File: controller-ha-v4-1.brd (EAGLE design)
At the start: 120 x 75 mm, 55 parts, among them IC2 LM358MX, U1 DS1307

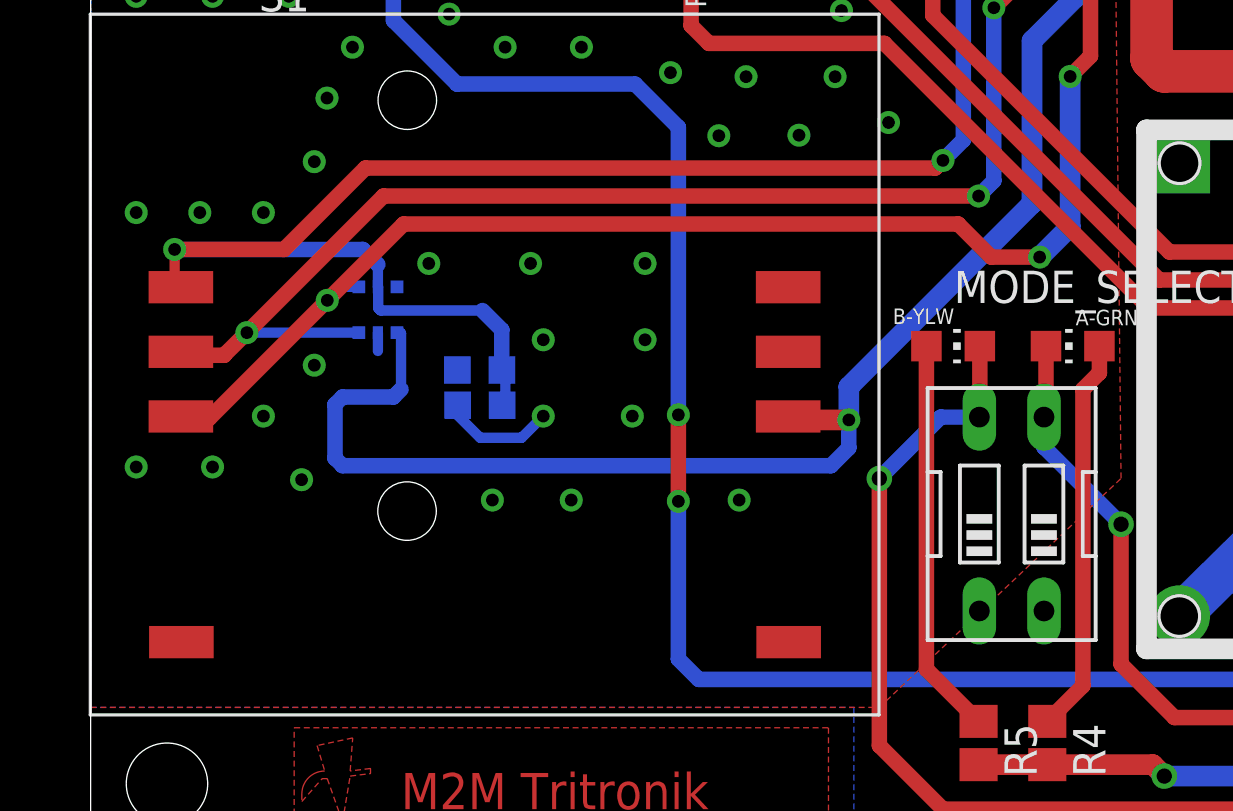
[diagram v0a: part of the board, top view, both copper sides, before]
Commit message: Revising Controller & IO Module
Some module (SIM900 & RTC) are not working, IO Module suddenly shorted
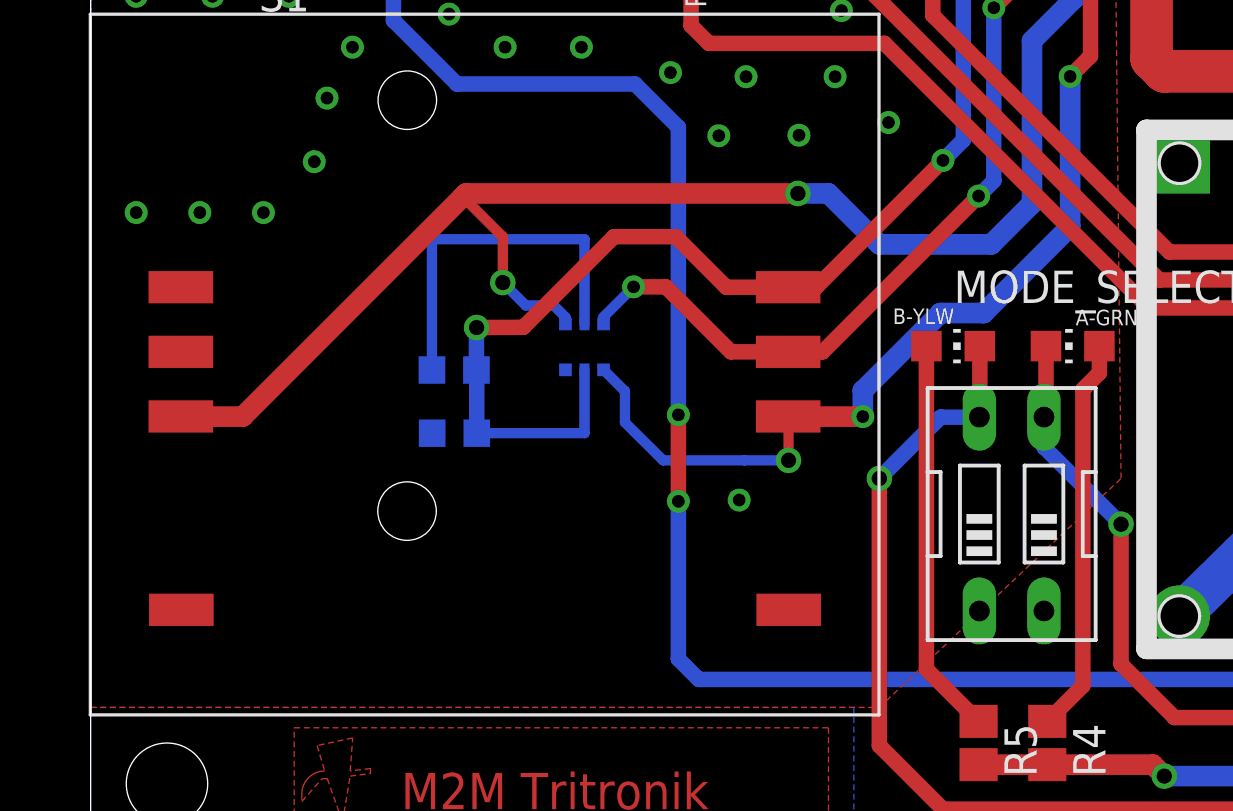
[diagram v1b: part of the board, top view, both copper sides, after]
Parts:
- moved D15 8.25 mm to (19.4, 20.2), turned to 180 degrees
- moved CSIM_100N 1.49 mm to (14.3, 16.8)
- moved CSIM_22P 1.00 mm to (14.3, 19.3)
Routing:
- net USIM_RESET: track 76.0 -> 56.1 mm
- net USIM_VCC: track 87.4 -> 69.1 mm
- net USIM_CLK: track 75.9 -> 61.2 mm
- net GND: track 15.2 -> 24.4 mm, vias 94 -> 80
- net USIM_DATA: track 75.8 -> 78.2 mm, vias 1 -> 2

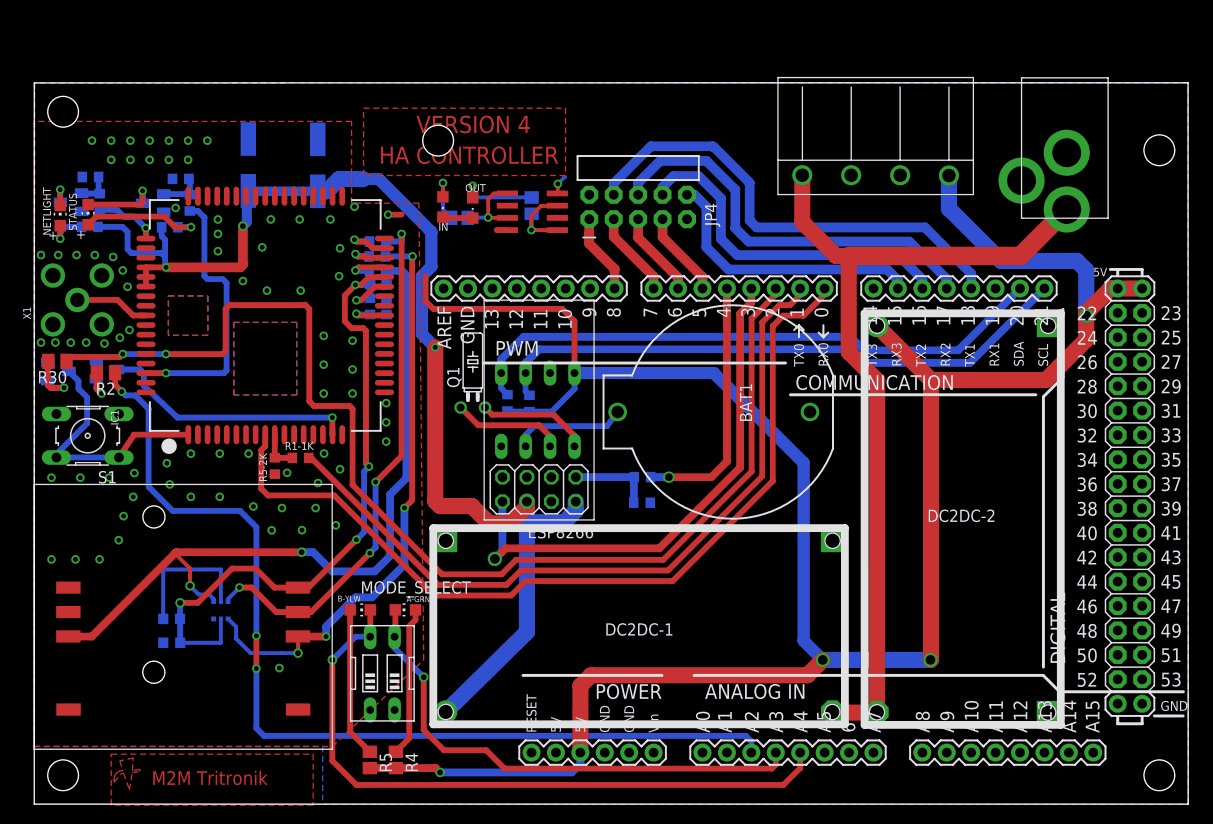
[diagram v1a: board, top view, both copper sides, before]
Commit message: Uptade all fixed design
This is whole new update for all device version
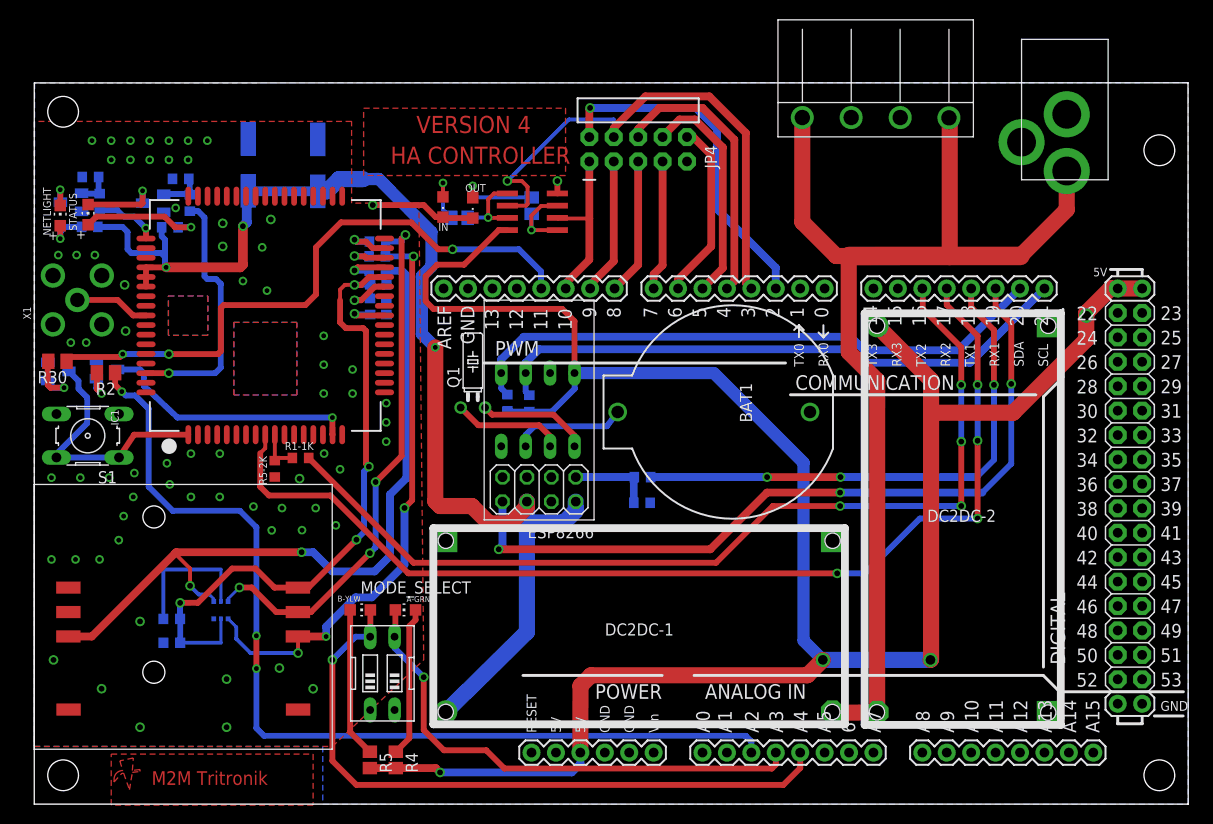
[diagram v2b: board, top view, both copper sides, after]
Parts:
- moved 4-WAY_L-TERMINAL 6.00 mm to (87.5, 75.5)
- moved JP4 6.00 mm to (62.8, 68.1)
- moved DC_JACKTHM 4.00 mm to (107.3, 75.1)
- moved R5-2K 0.30 mm to (25.0, 34.9)
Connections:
- removed net ESP_RXX: ARDUINO_FOOTPRINT.4, R1-1K1.2
- removed net SR_RST: ARDUINO_FOOTPRINT.15, JP4.10
- new net MR: ARDUINO_FOOTPRINT.6, JP4.10
- new net N$20: ARDUINO_FOOTPRINT.18, R1-1K1.2
- new net OE: ARDUINO_FOOTPRINT.2, JP4.2
- net +12V: now also 4-WAY_L-TERMINAL.1
- net CE: now also ARDUINO_FOOTPRINT.8; no longer ARDUINO_FOOTPRINT.6
- net CLK: now also ARDUINO_FOOTPRINT.9; no longer ARDUINO_FOOTPRINT.7
- net ESP_TX: now also ARDUINO_FOOTPRINT.19; no longer ARDUINO_FOOTPRINT.3
- net GND: no longer JP4.2
- net N$1: now also ARDUINO_FOOTPRINT.16; no longer ARDUINO_FOOTPRINT.1
- net PL: now also ARDUINO_FOOTPRINT.7; no longer ARDUINO_FOOTPRINT.5
- net PWRKEY: now also ARDUINO_FOOTPRINT.11; no longer ARDUINO_FOOTPRINT.2
- net Q7: now also ARDUINO_FOOTPRINT.10; no longer ARDUINO_FOOTPRINT.8
- net SHCP: now also ARDUINO_FOOTPRINT.5; no longer ARDUINO_FOOTPRINT.16
- net SIM_TX: now also ARDUINO_FOOTPRINT.17; no longer ARDUINO_FOOTPRINT.0
- net SR_DS: now also ARDUINO_FOOTPRINT.3; no longer ARDUINO_FOOTPRINT.18
- net STCP: now also ARDUINO_FOOTPRINT.4; no longer ARDUINO_FOOTPRINT.17
- net VCC: no longer 4-WAY_L-TERMINAL.1
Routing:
- net PWRKEY: track 122.6 -> 64.7 mm, vias 2 -> 3
- net N$20: track 0.00 -> 55.2 mm, vias 0 -> 3
- net OE: track 0.00 -> 36.3 mm, vias 0 -> 1
- net SR_RST: track 29.0 -> 0.00 mm
- net ESP_RXX: track 26.6 -> 0.00 mm, vias 1 -> 0
- net ESP_TX: track 54.8 -> 81.0 mm, vias 1 -> 3
- net +12V: track 89.2 -> 113.6 mm
- net N$1: track 79.1 -> 99.1 mm, vias 0 -> 4
- net SIM_TX: track 92.0 -> 111.6 mm, vias 0 -> 4
- net MR: track 0.00 -> 18.6 mm
- net VCC: track 241.9 -> 227.6 mm
- net STCP: track 42.7 -> 28.9 mm
- net SHCP: track 36.1 -> 23.8 mm
- net Q7: track 8.31 -> 17.6 mm
- net SR_DS: track 49.3 -> 55.9 mm, vias 0 -> 1
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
